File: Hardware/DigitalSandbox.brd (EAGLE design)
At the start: 109.2 x 76.2 mm, 80 parts, among them J1 AVR_SPI_PRG_6NS, Q1 MOSFET-N, Q2 MOSFET-P, U1 MCP73831, U2 ATMEGA328, U3 C2031N-1A2-B10K-GP, U4 MCP9700, U5 FT232RLSSOP, U6 LIGHTSENSORALS, U7 V_REG_LDOSMD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

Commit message: added Rev number
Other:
- outline, holes or cut-outs redrawn
- board text added: "v10"
- board text removed: "v03"
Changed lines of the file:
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@@
 <setting verticaltext="up"/>
 </settings>
-<grid distance="10" unitdist="mil" unit="mil" style="lines" multiple="1" display="yes" altdistance="0.005" altunitdist="inch" altunit="inch"/>
+<grid distance="5" unitdist="mil" unit="mil" style="lines" multiple="1" display="yes" altdistance="0.005" altunitdist="inch" altunit="inch"/>
 <layers>
 <layer number="1" name="Top" color="4" fill="1" visible="yes" active="yes"/>
@@
 <wire x1="33.528" y1="19.05" x2="8.5598" y2="19.05" width="0.2032" layer="20"/>
 <wire x1="42.8752" y1="27.305" x2="38.481" y2="19.685" width="0.2032" layer="20"/>
-<wire x1="16.9164" y1="29.21" x2="41.783" y2="29.21" width="0.2032" layer="20"/>
+<wire x1="17.0434" y1="29.21" x2="41.783" y2="29.21" width="0.2032" layer="20"/>
 <wire x1="48.9966" y1="35.2552" x2="52.1716" y2="38.4048" width="0.2032" layer="20"/>
 <wire x1="42.5704" y1="35.56" x2="42.291" y2="35.56" width="0.2032" layer="20"/>
@@
 <wire x1="53.1876" y1="20.32" x2="55.3973875" y2="19.0522875" width="0.2032" layer="20" curve="60.257051"/>
 <wire x1="53.1876" y1="20.32" x2="49.53" y2="26.67" width="0.2032" layer="20"/>
-<wire x1="16.9164" y1="33.02" x2="43.6118" y2="33.02" width="0.2032" layer="20"/>
+<wire x1="17.0434" y1="33.02" x2="43.6118" y2="33.02" width="0.2032" layer="20"/>
 <wire x1="58.039" y1="43.18" x2="56.4896" y2="43.18" width="0.2032" layer="20"/>
 <wire x1="86.106" y1="33.02" x2="94.615" y2="33.02" width="0.2032" layer="20"/>
@@
 <wire x1="83.82" y1="15.24" x2="82.55" y2="13.97" width="0.2032" layer="20" curve="90"/>
 <wire x1="14.605" y1="29.21" x2="14.605" y2="33.02" width="0.2032" layer="20"/>
-<wire x1="16.9164" y1="33.02" x2="16.9164" y2="29.21" width="0.2032" layer="20"/>
+<wire x1="17.0434" y1="33.02" x2="17.0434" y2="29.21" width="0.2032" layer="20"/>
 <wire x1="60.071" y1="67.056" x2="60.071" y2="61.7728" width="0.2032" layer="20"/>
 <wire x1="58.039" y1="61.7728" x2="58.039" y2="67.056" width="0.2032" layer="20"/>
@@
 <wire x1="0" y1="2.54" x2="2.54" y2="0" width="0.2032" layer="20" curve="90"/>
 <text x="48.26" y="-7.62" size="1.778" layer="25">Casey Kuhns</text>
-<text x="103.632" y="0.508" size="1.27" layer="16" font="vector" ratio="20" rot="MR0">v03</text>
+<text x="103.632" y="0.508" size="1.27" layer="16" font="vector" ratio="20" rot="MR0">v10</text>
 <polygon width="0.001" layer="21">
 <vertex x="41.0694" y="68.9322"/>
@@
 </class>
 </classes>
-<designrules name="default">
+<designrules name="SparkFun-2-layer">
 <description language="en">&lt;b&gt;EAGLE Design Rules&lt;/b&gt;
 &lt;p&gt;
@@
 <param name="mdViaViaSameLayer" value="8mil"/>
 <param name="mnLayersViaInSmd" value="2"/>
-<param name="mdCopperDimension" value="10mil"/>
+<param name="mdCopperDimension" value="8mil"/>
 <param name="mdDrill" value="8mil"/>
 <param name="mdSmdStop" value="0mil"/>
-<param name="msWidth" value="6mil"/>
+<param name="msWidth" value="7mil"/>
 <param name="msDrill" value="15mil"/>
 <param name="msMicroVia" value="9.99mm"/>
@@
 <param name="dpGapFactor" value="2.5"/>
 <param name="checkGrid" value="0"/>
-<param name="checkAngle" value="1"/>
+<param name="checkAngle" value="0"/>
 <param name="checkFont" value="1"/>
 <param name="checkRestrict" value="1"/>

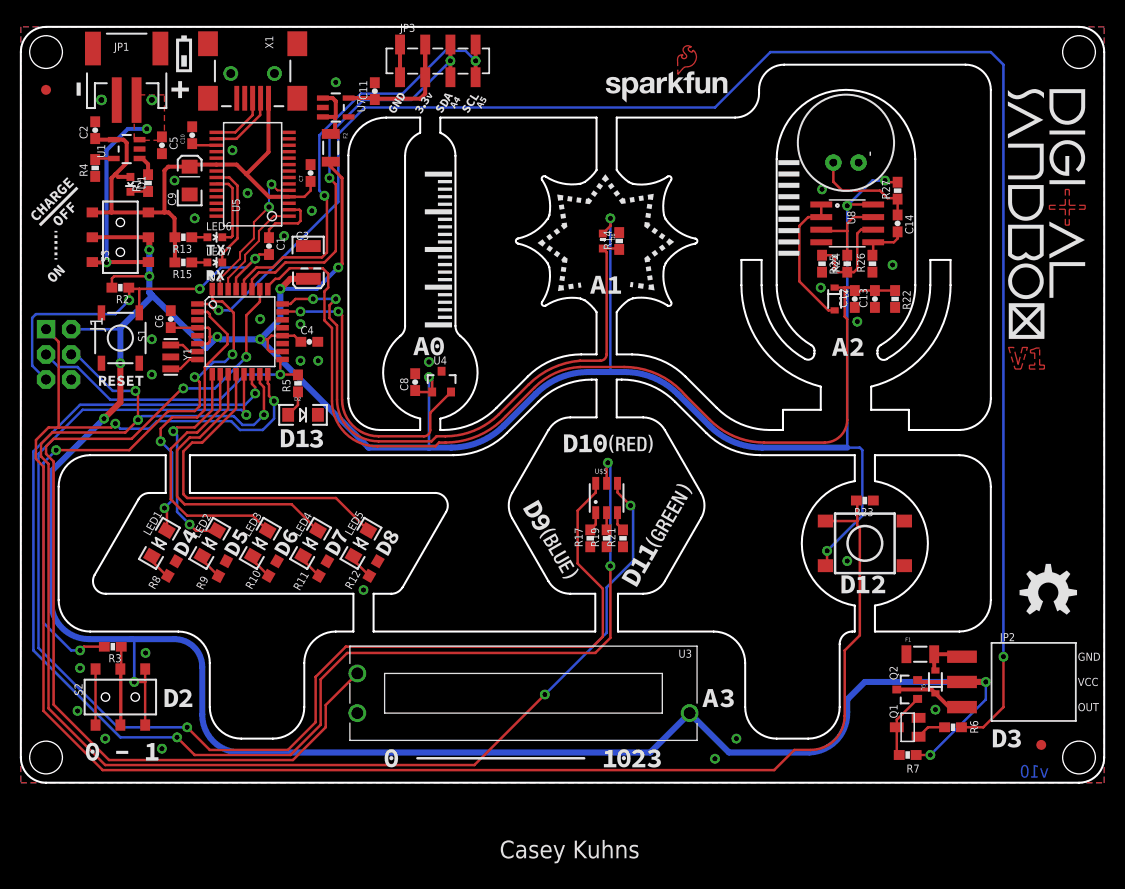
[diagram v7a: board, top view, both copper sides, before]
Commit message: reduced size of board by .15 inch in X
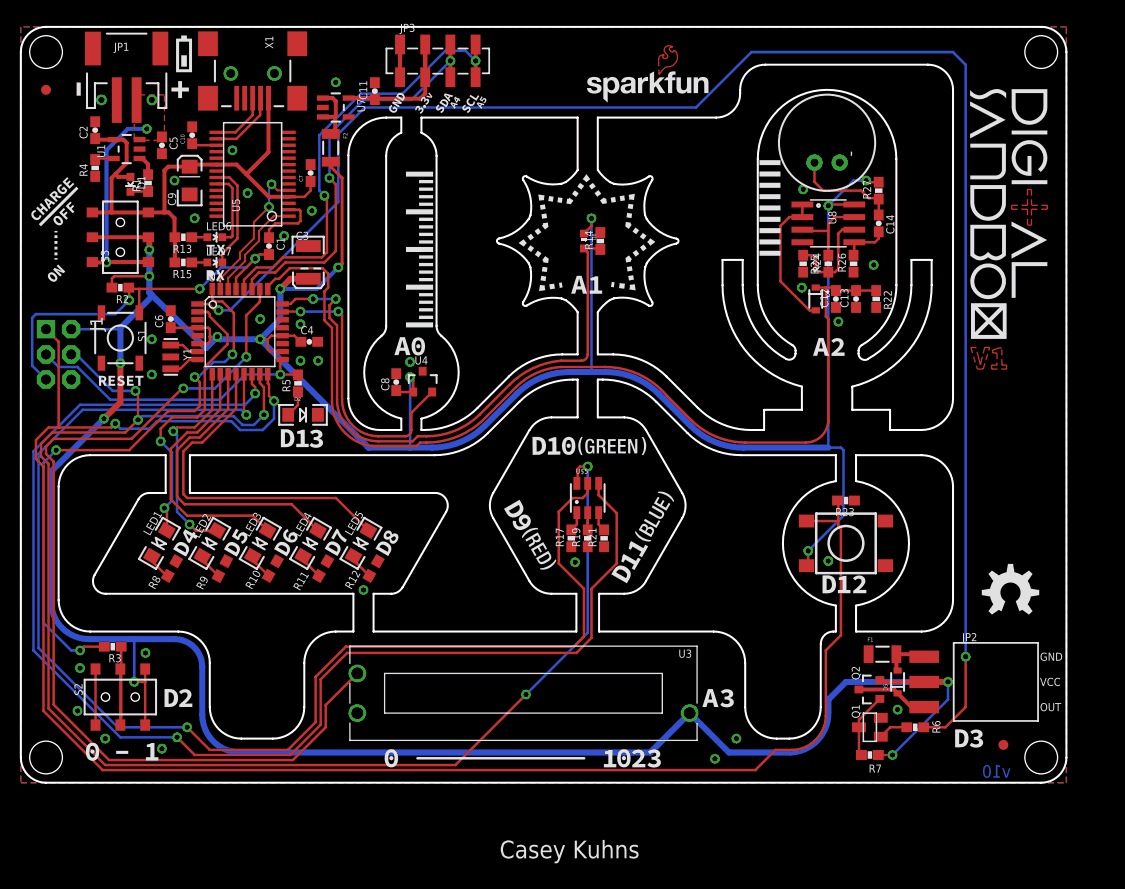
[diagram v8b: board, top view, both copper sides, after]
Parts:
- moved D5 3.81 mm to (88.4, 10.2)
- moved F1 3.81 mm to (86.9, 13.0)
- moved FID1 3.81 mm to (99.1, 3.81)
- moved JP2 3.81 mm to (98.3, 10.2)
- moved Q1 3.81 mm to (85.6, 5.59)
- moved Q2 3.81 mm to (85.6, 9.40)
- moved R6 3.81 mm to (90.2, 5.59)
- moved R7 3.81 mm to (85.6, 2.79)
- moved STANDOFF1 3.81 mm to (102.9, 73.7)
- moved STANDOFF2 3.81 mm to (102.9, 2.54)
- moved C12 1.91 mm to (82.2, 48.8)
- moved C13 1.91 mm to (84.2, 48.8)
- moved C14 1.91 mm to (86.5, 56.4)
- moved C8 1.91 mm to (37.8, 40.4)
- moved D4 1.91 mm to (80.1, 48.8)
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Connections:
- removed net N$28: R19.2, U$5.CR
- new net BLUE: R17.2, U$5.CB
- net D10: now also U$5.AG; no longer U$5.AR
- net D11: now also U$5.AB; no longer U$5.AG
- net D9: now also U$5.AR; no longer U$5.AB
- net RED: now also R19.2, U$5.CR; no longer R17.2, U$5.CB
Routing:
- net VCC: track 396.8 -> 391.1 mm
- net D10: track 137.1 -> 132.7 mm, vias 4 -> 2
- net D3: track 166.7 -> 162.9 mm
- net BLUE: track 0.00 -> 1.97 mm
- net A2: track 99.6 -> 97.7 mm
- net A1: track 60.4 -> 58.5 mm
- net A0: track 30.0 -> 28.1 mm
- net D12: track 180.1 -> 178.2 mm
- net N$28: track 1.74 -> 0.00 mm
- net D9: track 132.6 -> 131.7 mm
- net GND: vias 29 -> 30
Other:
- board size 109.2 x 76.2 mm -> 105.4 x 76.2 mm
